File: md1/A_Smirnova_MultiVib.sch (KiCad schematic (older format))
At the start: 10 parts, among them Q1 FFB2222A

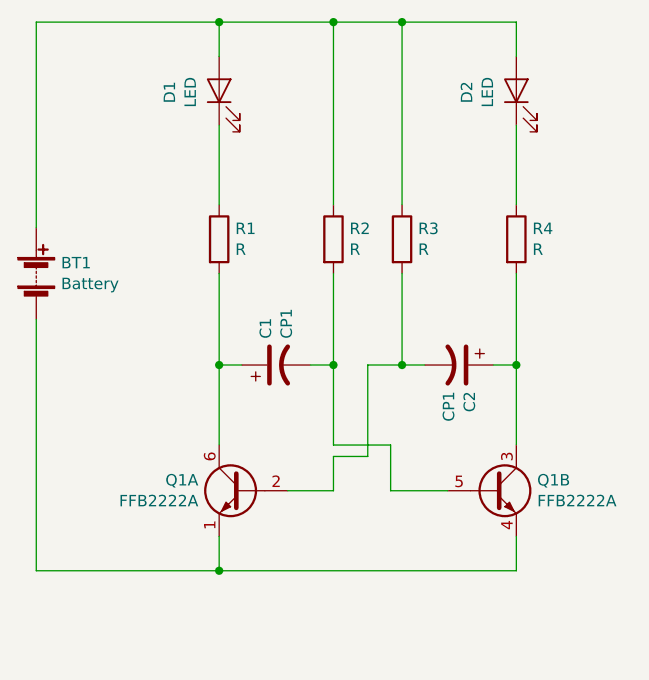
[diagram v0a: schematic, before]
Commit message: Dual tranzistora izveide
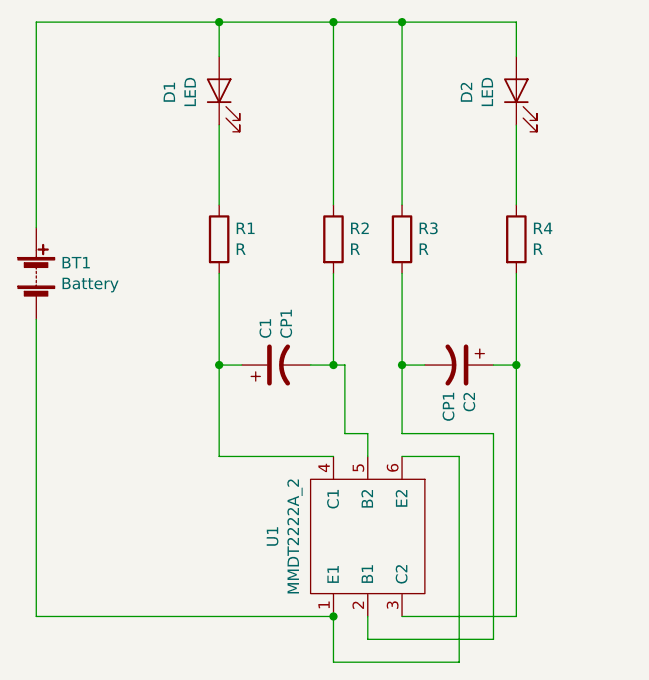
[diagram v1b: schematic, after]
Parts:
- removed Q1: FFB2222A, Package_TO_SOT_SMD:SOT-363_SC-70-6, symbol Transistor_BJT:FFB2222A
- added U1: MMDT2222A_2, symbol Dual_NPN_Transistor:MMDT2222A_2
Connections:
- net at BT1.2 (-): now also U1.1 (E1), U1.6 (E2)
- net at C2.1, R4.2: now also U1.3 (C2)
- net at C2.2, R3.2: now also U1.2 (B1)
- net at C1.1, R1.2: now also U1.4 (C1)
- net at C1.2, R2.2: now also U1.5 (B2)
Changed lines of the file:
@@
 	2400 950  2400 1850
-Wire Wire Line
-	2400 2250 2400 3350
-Wire Wire Line
-	2400 3350 3200 3350
-Wire Wire Line
-	4500 3350 4500 3200
-Wire Wire Line
-	4500 2800 4500 2450
 Wire Wire Line
 	4500 1750 4500 1400
@@
 Wire Wire Line
 	3700 950  4000 950
-Wire Wire Line
-	3200 3200 3200 3350
-Connection ~ 3200 3350
-Wire Wire Line
-	3200 3350 4500 3350
-Wire Wire Line
-	3200 2800 3200 2450
 Connection ~ 3200 950
 Wire Wire Line
@@
 Wire Wire Line
 	3700 2450 3600 2450
-Wire Wire Line
-	3850 2450 3850 2850
-Wire Wire Line
-	3850 2850 3700 2850
-Wire Wire Line
-	3700 2850 3700 3000
-Wire Wire Line
-	3700 3000 3500 3000
-Wire Wire Line
-	3850 2450 4000 2450
 Connection ~ 4000 2450
 Wire Wire Line
 	4000 2450 4100 2450
+$Comp
+L Dual_NPN_Transistor:MMDT2222A_2 U1
+U 1 1 5F7F92E7
+P 3900 3200
+F 0 "U1" H 3900 3665 50  0000 C CNN
+F 1 "MMDT2222A_2" H 3900 3574 50  0000 C CNN
+F 2 "" H 3950 2850 50  0001 C CNN
+F 3 "" H 3950 2850 50  0001 C CNN
+	1    3900 3200
+	0    -1   -1   0
+$EndComp
 Wire Wire Line
-	3700 2450 3700 2800
+	2400 3550 3700 3550
 Wire Wire Line
-	3700 2800 3950 2800
+	2400 2250 2400 3550
 Wire Wire Line
-	3950 2800 3950 3000
+	4000 2850 4250 2850
 Wire Wire Line
-	3950 3000 4200 3000
+	4250 2850 4250 3750
+Wire Wire Line
+	4250 3750 3700 3750
+Wire Wire Line
+	3700 3750 3700 3550
+Connection ~ 3700 3550
+Wire Wire Line
+	3700 2850 3200 2850
+Wire Wire Line
+	3200 2450 3200 2850
+Wire Wire Line
+	4500 2450 4500 3550
+Wire Wire Line
+	4000 3550 4500 3550
+Wire Wire Line
+	3850 3550 3850 3650
+Wire Wire Line
+	3850 3650 4400 3650
+Wire Wire Line
+	4400 3650 4400 2750
+Wire Wire Line
+	4400 2750 4000 2750
+Wire Wire Line
+	4000 2750 4000 2450
+Wire Wire Line
+	3750 2450 3750 2750
+Wire Wire Line
+	3750 2750 3850 2750
+Wire Wire Line
+	3850 2750 3850 2850
+Wire Wire Line
+	3750 2450 3700 2450
 Connection ~ 3700 2450
-$Comp
-L Transistor_BJT:FFB2222A Q1
-U 1 1 5F7EB267
-P 3300 3000
-F 0 "Q1" H 3491 3046 50  0000 L CNN
-F 1 "FFB2222A" H 3491 2955 50  0000 L CNN
-F 2 "Package_TO_SOT_SMD:SOT-363_SC-70-6" H 3500 3100 50  0001 C CNN
-F 3 "https://www.fairchildsemi.com/datasheets/FF/FFB2222A.pdf" H 3300 3000 50  0001 C CNN
-	1    3300 3000
-	-1   0    0    -1
-$EndComp
-$Comp
-L Transistor_BJT:FFB2222A Q1
-U 2 1 5F7EBEE2
-P 4400 3000
-F 0 "Q1" H 4591 3046 50  0000 L CNN
-F 1 "FFB2222A" H 4591 2955 50  0000 L CNN
-F 2 "Package_TO_SOT_SMD:SOT-363_SC-70-6" H 4600 3100 50  0001 C CNN
-F 3 "https://www.fairchildsemi.com/datasheets/FF/FFB2222A.pdf" H 4400 3000 50  0001 C CNN
-	2    4400 3000
-	1    0    0    -1
-$EndComp
 $EndSCHEMATC
